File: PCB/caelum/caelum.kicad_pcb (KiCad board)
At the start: 2 copper layers, 54 x 39.5 mm, 26 parts, among them J1 Conn_01x06_Pin, J10 Conn_01x04_Pin, J3 Pulse1, J4 Batt, J6 Pulse2, J7 Conn_01x04_Pin, J8 DS18B20, Q1 FS8205A-FC, U1 DW01A, U2 MCP1700T-3302E, U3 ESP32-H2-SUPERMINI

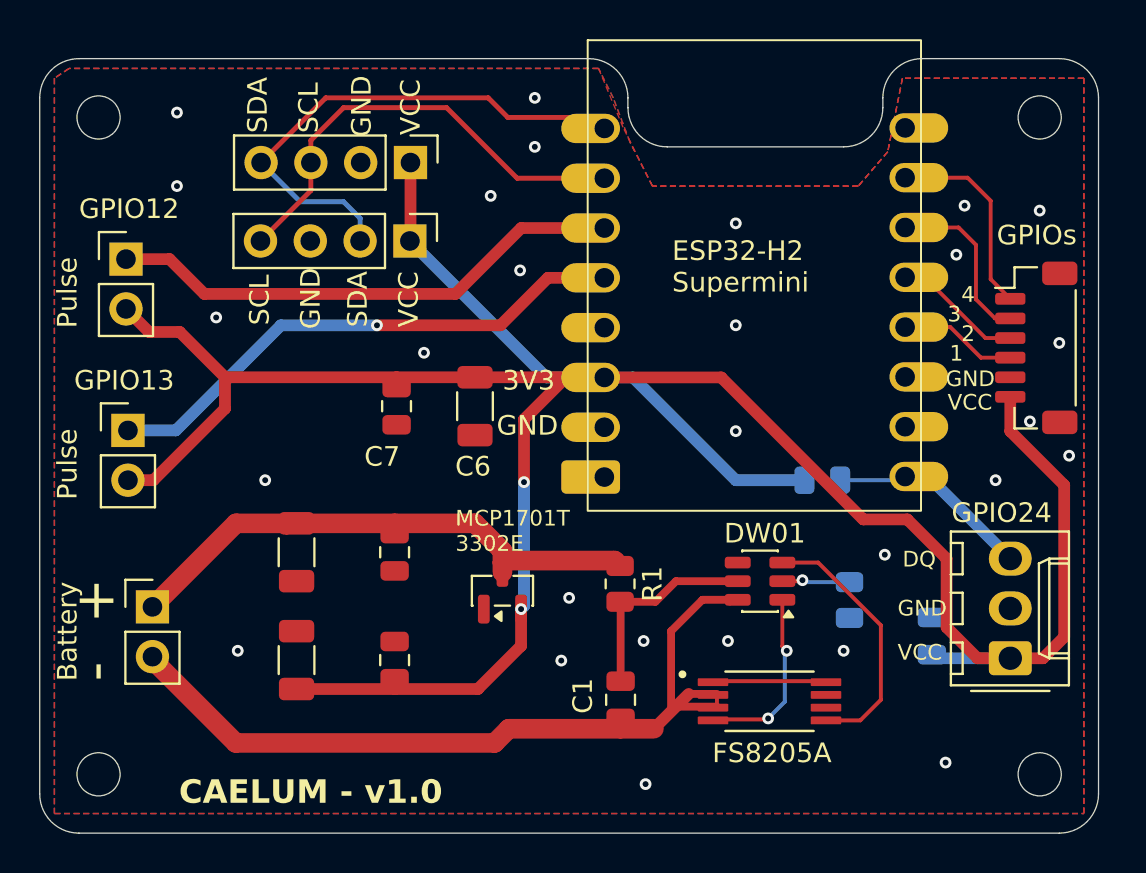
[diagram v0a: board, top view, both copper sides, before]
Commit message: Refactor PCB design files: reset column widths, clear DRC exclusions, and add new junctions and wires
- Reset column widths in `caelum.kicad_prl` to zero.
- Cleared DRC exclusions in `caelum.kicad_pro`.
- Added multiple junctions and wires in `caelum.kicad_sch` to enhance circuit connectivity.
- Introduced new components (resistors and capacitors) with updated properties and references.
- Added global labels for GPIO and power connections to improve schematic clarity.
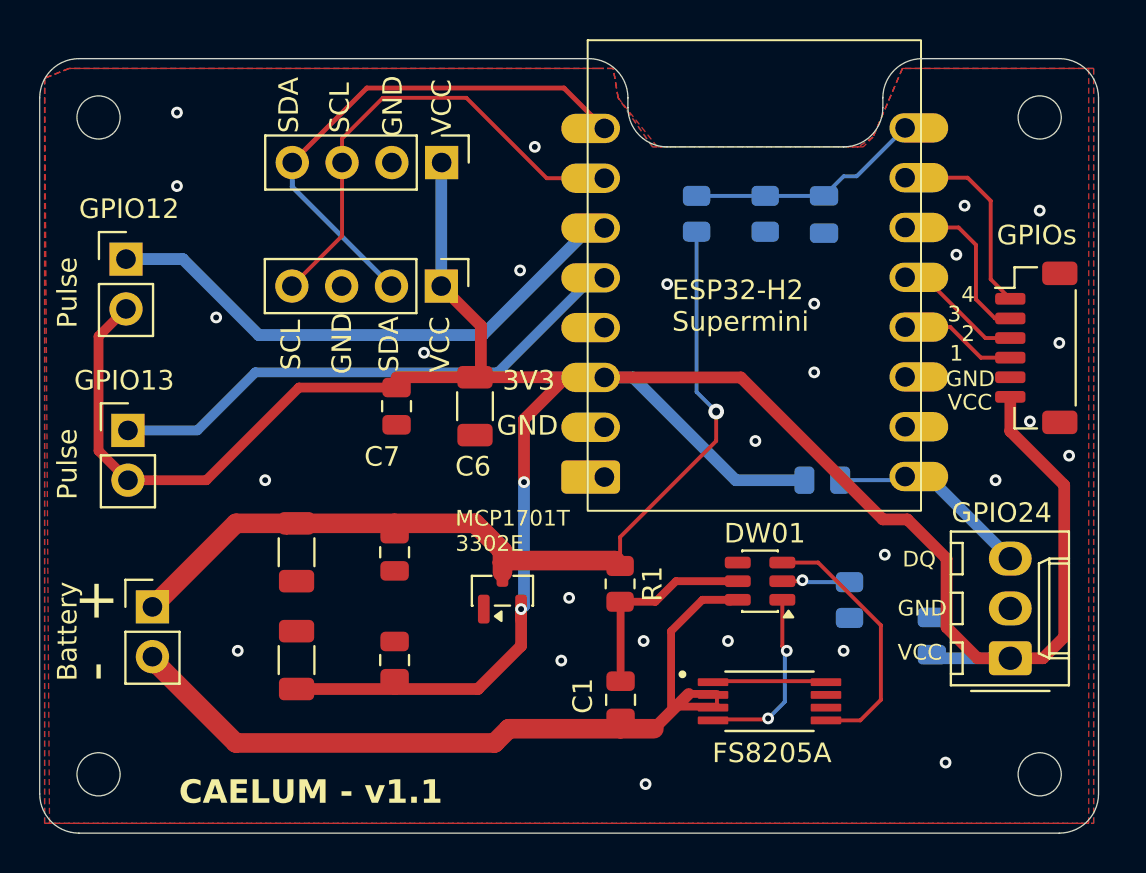
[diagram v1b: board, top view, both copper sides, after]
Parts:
- added C9: 0.1µF, Capacitor_SMD:C_0805_2012Metric, B.Cu at (97.0, 34.5)
- added R4: 100K, Resistor_SMD:R_0805_2012Metric, B.Cu at (90.5, 34.4)
- added R5: 100K, Resistor_SMD:R_0805_2012Metric, B.Cu at (94.0, 34.4)
- moved J7 2.80 mm to (77.5, 38.1)
- moved J10 1.59 mm to (77.5, 31.8)
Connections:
- U3 pad 12: unconnected-(U3-IO5-Pad12) -> GPIO5
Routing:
- net BATT+: track 28.2 -> 47.7 mm, vias 0 -> 1
- net GPIO5: track 0.00 -> 12.1 mm
- net GPIO12: track 26.5 -> 28.3 mm
- net GPIO13: track 27.5 -> 29.0 mm, vias 1 -> 0
- net SCL: track 23.3 -> 24.5 mm
- net OUT-: vias 28 -> 27
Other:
- board text added: "CAELUM - v1.1"
- board text removed: "CAELUM - v1.0"
